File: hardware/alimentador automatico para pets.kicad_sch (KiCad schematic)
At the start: 24 parts, among them J1 Conn_01x02, J2 Conn_01x04, J3 Conn_01x03, J4 Conn_01x03, J5 Conn_01x02, J6 Conn_01x05, J7 Conn_01x02, J8 Conn_01x04, SW1 SW_Push, SW2 SW_Push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

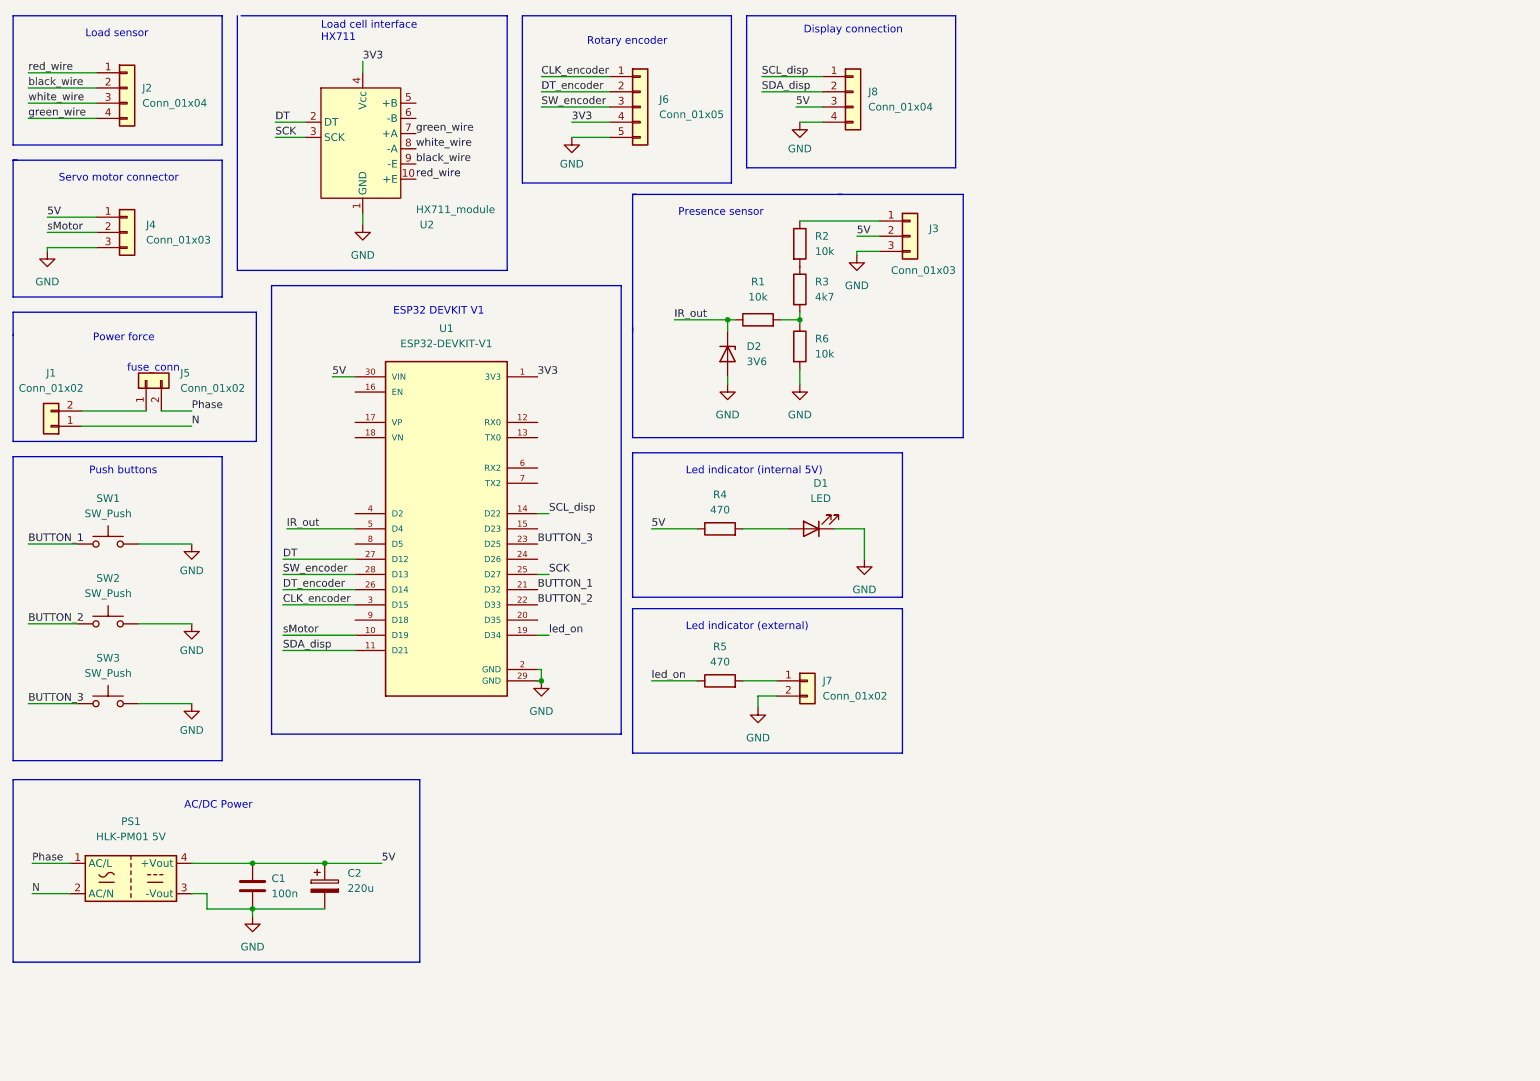
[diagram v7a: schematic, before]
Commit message: removing leds and changing components positions #14
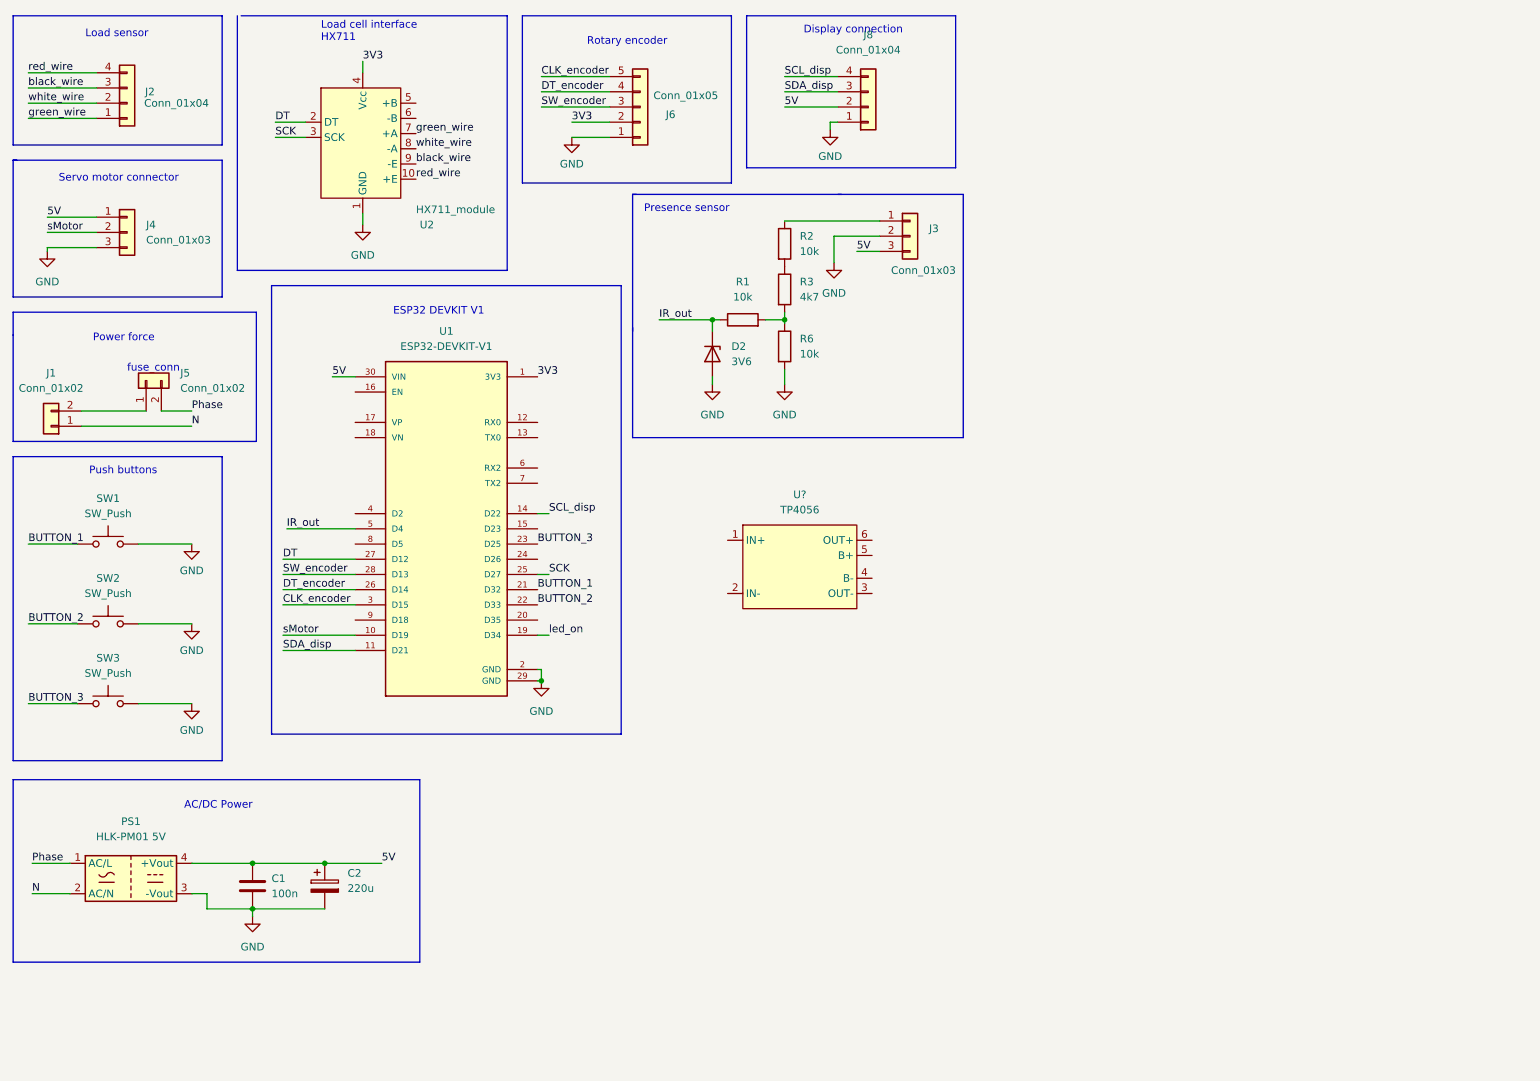
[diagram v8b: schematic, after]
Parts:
- removed D1: LED, LED_THT:LED_D3.0mm, symbol Device:LED
- removed J7: Conn_01x02, Connector_PinSocket_2.54mm:PinSocket_1x02_P2.54mm_Vertical, symbol Connector_Generic:Conn_01x02
- removed R4, R5: 470, Resistor_THT:R_Axial_DIN0207_L6.3mm_D2.5mm_P7.62mm_Horizontal, symbol Device:R
- added U?: TP4056, symbol symbol_lib:TP4056
- J1: footprint Connector_PinSocket_2.54mm:PinSocket_1x02_P2.54mm_Vertical -> Connector_Wire:SolderWire-0.1sqmm_1x02_P3.6mm_D0.4mm_OD1mm_Relief
- J2: footprint Connector_PinSocket_2.54mm:PinSocket_1x04_P2.54mm_Vertical -> Connector_Wire:SolderWire-0.1sqmm_1x04_P3.6mm_D0.4mm_OD1mm_Relief
- J5: footprint Connector_PinSocket_2.54mm:PinSocket_1x02_P2.54mm_Vertical -> Connector_Wire:SolderWire-0.1sqmm_1x02_P3.6mm_D0.4mm_OD1mm
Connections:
- net 3V3: now also J6.2 (Pin_2); no longer J6.4 (Pin_4)
- net 5V: now also J3.3 (Pin_3), J8.2 (Pin_2); no longer J3.2 (Pin_2), J8.3 (Pin_3)
- net CLK_encoder: now also J6.5 (Pin_5); no longer J6.1 (Pin_1)
- net DT_encoder: now also J6.4 (Pin_4); no longer J6.2 (Pin_2)
- net GND: now also J3.2 (Pin_2), J6.1 (Pin_1), J8.1 (Pin_1); no longer J3.3 (Pin_3), J6.5 (Pin_5), J8.4 (Pin_4)
- net SCL_disp: now also J8.4 (Pin_4); no longer J8.1 (Pin_1)
- net SDA_disp: now also J8.3 (Pin_3); no longer J8.2 (Pin_2)
- net black_wire: now also J2.3 (Pin_3); no longer J2.2 (Pin_2)
- net green_wire: now also J2.1 (Pin_1); no longer J2.4 (Pin_4)
- net red_wire: now also J2.4 (Pin_4); no longer J2.1 (Pin_1)
- net white_wire: now also J2.2 (Pin_2); no longer J2.3 (Pin_3)
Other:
- note removed: "Led indicator (external)"
- note removed: "Led indicator (internal 5V)"
- moved on the sheet: D2, J8, R1, R2, R3, R6
